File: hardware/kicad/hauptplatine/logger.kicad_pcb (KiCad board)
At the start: 4 copper layers, 121 x 121 mm, 4 parts

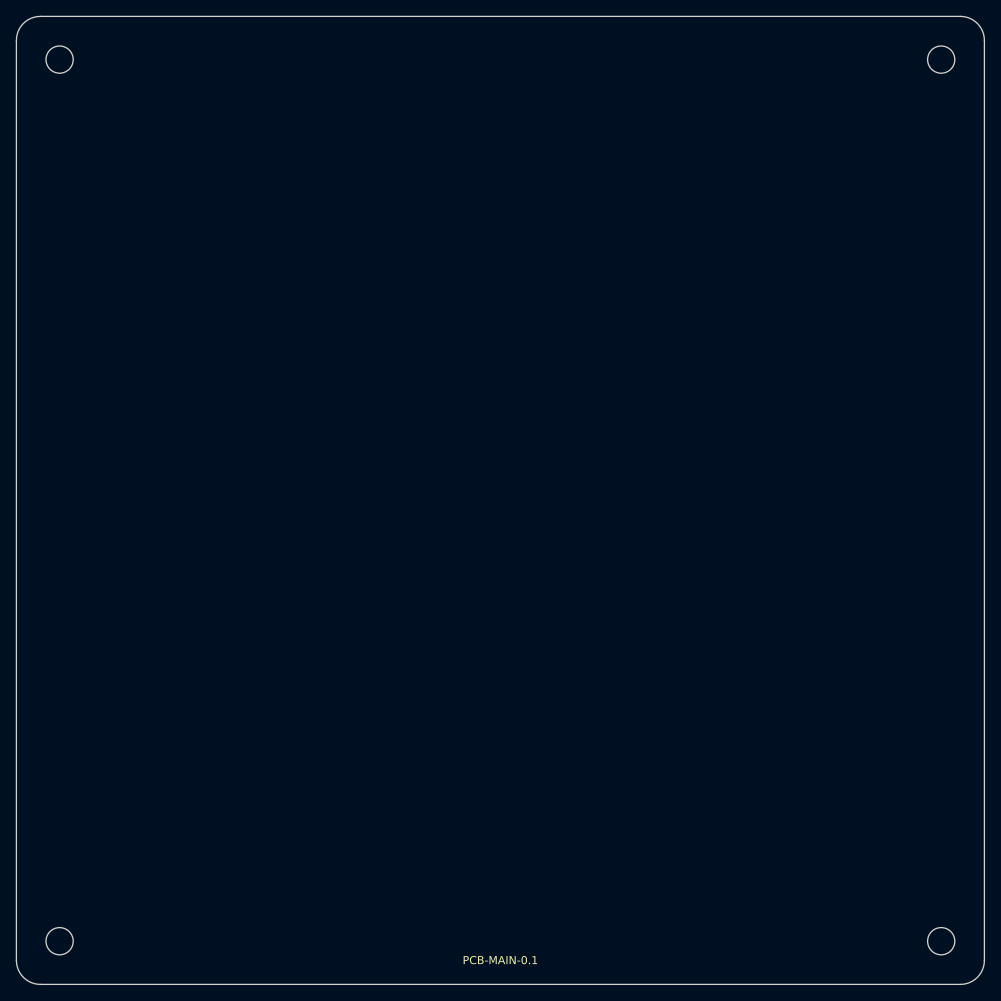
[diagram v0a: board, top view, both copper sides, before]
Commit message: update
"Hauptplatine grob platziert (platine_bestuecken.py, 139 Bauteile, Schaltplanabgleich 0); Gehäuse mit STEP geprüft: Lochbild bestätigt, Freiraum über Platine >= 44,3 mm (HW-03 erfüllt), Dombohrung Ø 2,4 mm korrigiert, Lichtleiter ca. 19,4 mm. Tests: ERC 0, Netzprüfung 178/178, alle_tests_linux.sh rc=0"
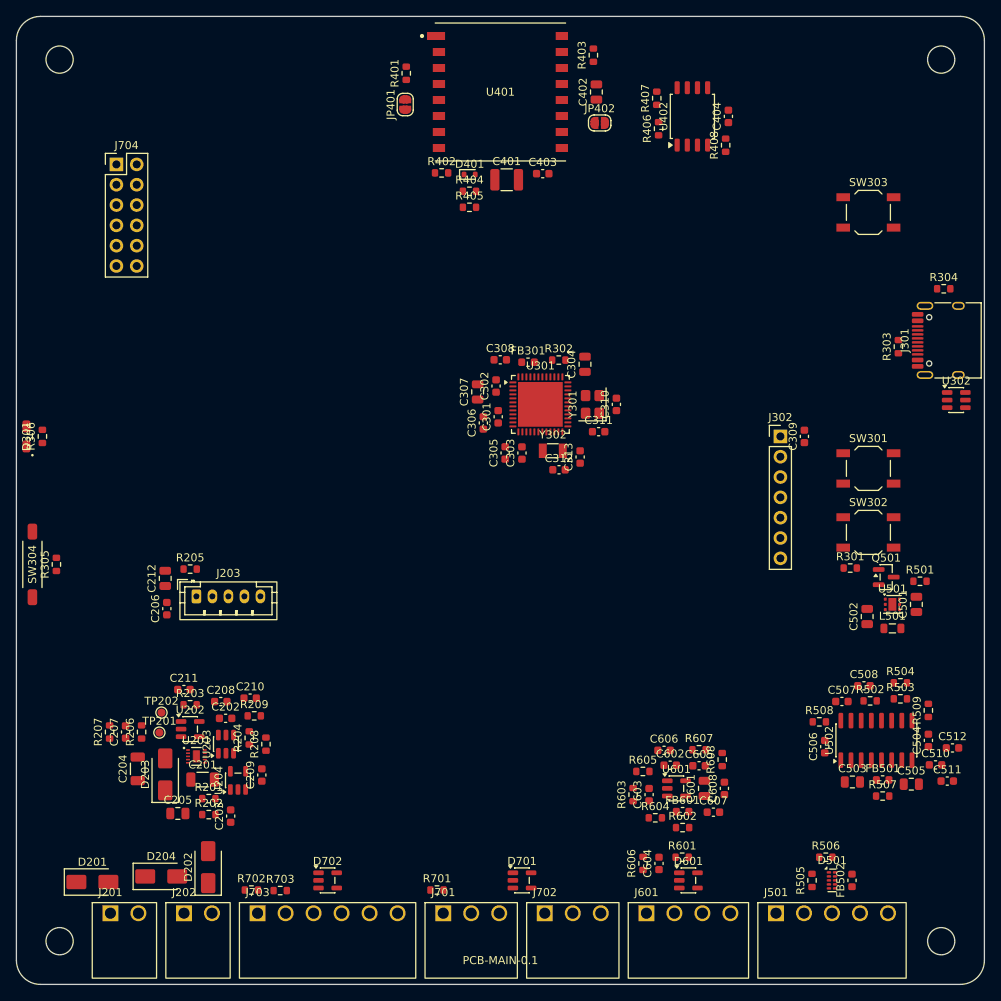
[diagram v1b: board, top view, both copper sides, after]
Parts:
- added C201: 4,7µ 50V X7R, Capacitor_SMD:C_1206_3216Metric, F.Cu at (62.8, 134.9)
- added C202: 100n 50V, Capacitor_SMD:C_0603_1608Metric, F.Cu at (65.7, 127.2)
- added C203: 100n, Capacitor_SMD:C_0603_1608Metric, F.Cu at (66.3, 139.5)
- added C204: 22µ 25V X5R, Capacitor_SMD:C_1206_3216Metric, F.Cu at (54.7, 133.6)
- added C205: 4,7µ, Capacitor_SMD:C_0805_2012Metric, F.Cu at (59.7, 139.1)
- added C206: 10n, Capacitor_SMD:C_0603_1608Metric, F.Cu at (58.3, 113.5)
- added C207: 100n, Capacitor_SMD:C_0603_1608Metric, F.Cu at (53.1, 128.9)
- added C208: 2,2µ 16V X7R, Capacitor_SMD:C_0603_1608Metric, F.Cu at (65.1, 125.1)
- added C209: 2,2µ 16V X7R, Capacitor_SMD:C_0603_1608Metric, F.Cu at (70.2, 134.3)
- added C210: 1n, Capacitor_SMD:C_0603_1608Metric, F.Cu at (68.7, 124.7)
- added C211: 1µ, Capacitor_SMD:C_0603_1608Metric, F.Cu at (60.4, 123.6)
- added C212: 4,7µ 16V X7R, Capacitor_SMD:C_0805_2012Metric, F.Cu at (58.1, 109.8)
- added C301: 100n, Capacitor_SMD:C_0603_1608Metric, F.Cu at (99.7, 89.5)
- added C302: 100n, Capacitor_SMD:C_0603_1608Metric, F.Cu at (99.5, 85.7)
- added C303: 100n, Capacitor_SMD:C_0603_1608Metric, F.Cu at (102.7, 94.1)
- added C304: 10µ 10V X5R, Capacitor_SMD:C_0805_2012Metric, F.Cu at (110.6, 83.0)
- added C305: 100n, Capacitor_SMD:C_0603_1608Metric, F.Cu at (100.6, 94.1)
- added C306: 1µ, Capacitor_SMD:C_0603_1608Metric, F.Cu at (97.9, 90.3)
- added C307: 4,7µ X7R, Capacitor_SMD:C_0805_2012Metric, F.Cu at (97.2, 86.4)
- added C308: 100n, Capacitor_SMD:C_0603_1608Metric, F.Cu at (100.0, 82.4)
- added C309: 100n, Capacitor_SMD:C_0603_1608Metric, F.Cu at (138.0, 92.0)
- added C310: 18p C0G, Capacitor_SMD:C_0603_1608Metric, F.Cu at (114.5, 88.0)
- added C311: 18p C0G, Capacitor_SMD:C_0603_1608Metric, F.Cu at (112.3, 91.4)
- added C312: 8,2p C0G, Capacitor_SMD:C_0603_1608Metric, F.Cu at (107.3, 96.2)
- added C313: 8,2p C0G, Capacitor_SMD:C_0603_1608Metric, F.Cu at (110.0, 94.6)
- added C401: 100µ 6,3V X5R, Capacitor_SMD:C_1210_3225Metric, F.Cu at (100.8, 59.9)
- added C402: 10µ 10V X5R, Capacitor_SMD:C_0805_2012Metric, F.Cu at (112.0, 49.0)
- added C403: 100n, Capacitor_SMD:C_0603_1608Metric, F.Cu at (105.3, 59.2)
- added C404: 100n, Capacitor_SMD:C_0603_1608Metric, F.Cu at (128.5, 52.0)
- added C501: 4,7µ 16V X5R, Capacitor_SMD:C_0805_2012Metric, F.Cu at (152.0, 113.0)
- added C502: 10µ 10V X5R, Capacitor_SMD:C_0805_2012Metric, F.Cu at (145.8, 114.5)
- added C503: 10µ 10V X5R, Capacitor_SMD:C_0805_2012Metric, F.Cu at (144.0, 135.2)
- added C504: 100n, Capacitor_SMD:C_0603_1608Metric, F.Cu at (153.5, 130.0)
- added C505: 10µ 10V X5R, Capacitor_SMD:C_0805_2012Metric, F.Cu at (151.4, 135.5)
- added C506: 100n, Capacitor_SMD:C_0603_1608Metric, F.Cu at (140.5, 130.8)
- added C507: 100n, Capacitor_SMD:C_0603_1608Metric, F.Cu at (142.7, 125.1)
- added C508: 100n, Capacitor_SMD:C_0603_1608Metric, F.Cu at (145.4, 123.2)
- added C510: 100n, Capacitor_SMD:C_0603_1608Metric, F.Cu at (154.4, 133.1)
- added C511: 10n C0G, Capacitor_SMD:C_0603_1608Metric, F.Cu at (155.9, 135.1)
- added C512: 10n C0G, Capacitor_SMD:C_0603_1608Metric, F.Cu at (156.5, 130.9)
- added C601: 22µ 10V X5R, Capacitor_SMD:C_0805_2012Metric, F.Cu at (125.5, 136.0)
- added C602: 100n, Capacitor_SMD:C_0603_1608Metric, F.Cu at (121.2, 133.1)
- added C603: 1µ, Capacitor_SMD:C_0603_1608Metric, F.Cu at (118.6, 136.8)
- added C604: 220n X7R, Capacitor_SMD:C_0603_1608Metric, F.Cu at (119.8, 145.4)
- added C605: 22n C0G, Capacitor_SMD:C_0603_1608Metric, F.Cu at (124.8, 133.2)
- added C606: 10n C0G, Capacitor_SMD:C_0603_1608Metric, F.Cu at (120.5, 131.2)
- added C607: 100n, Capacitor_SMD:C_0603_1608Metric, F.Cu at (126.6, 139.0)
- added C608: 10n C0G, Capacitor_SMD:C_0603_1608Metric, F.Cu at (128.0, 136.0)
- added D201: SS34, Diode_SMD:D_SMA, F.Cu at (49.0, 147.7)
- added D202: SS34, Diode_SMD:D_SMA, F.Cu at (63.5, 145.8)
- added D203: SS34, Diode_SMD:D_SMA, F.Cu at (58.1, 134.2)
- added D204: SMAJ12A, Diode_SMD:D_SMA, F.Cu at (57.6, 147.0)
- added D301: LTST-S220KGKT, Bienen:LED_Lite-On_LTST-S220_SideView, F.Cu at (40.8, 92.0)
- added D401: TVS 3,3V, Diode_SMD:D_SOD-523, F.Cu at (96.2, 59.3)
- added D501: TPD4E05U06DQAR, Package_SON:USON-10_2.5x1.0mm_P0.5mm, F.Cu at (141.4, 147.5)
- added D601: ESDS304DBVR, Package_TO_SOT_SMD:SOT-23-5, F.Cu at (123.5, 147.5)
- added D701: ESDS304DBVR, Package_TO_SOT_SMD:SOT-23-5, F.Cu at (102.7, 147.5)
- added D702: ESDS304DBVR, Package_TO_SOT_SMD:SOT-23-5, F.Cu at (78.4, 147.5)
- added FB301: 600R@100MHz, Inductor_SMD:L_0603_1608Metric, F.Cu at (103.5, 82.7)
- added FB501: 600R@100MHz, Inductor_SMD:L_0603_1608Metric, F.Cu at (147.8, 134.9)
- added FB502: Ferrit ≤ 0,1 Ω, Inductor_SMD:L_0603_1608Metric, F.Cu at (143.9, 147.5)
- added FB601: 600R@100MHz, Inductor_SMD:L_0603_1608Metric, F.Cu at (122.8, 138.9)
- added J201: Solar 1, Bienen:DEGSON_15EDGRC-3.5-02P, F.Cu at (51.2, 151.6)
- added J202: Solar 2, Bienen:DEGSON_15EDGRC-3.5-02P, F.Cu at (60.4, 151.6)
- added J203: Akku (JST PH 5), Connector_JST:JST_PH_B5B-PH-K_1x05_P2.00mm_Vertical, F.Cu at (62.0, 112.0)
- added J301: USB-C, Connector_USB:USB_C_Receptacle_HRO_TYPE-C-31-M-12, F.Cu at (156.2, 80.0)
- added J302: Debug (SWD + Serial1), Connector_PinHeader_2.54mm:PinHeader_1x07_P2.54mm_Vertical, F.Cu at (135.0, 92.0)
- added J501: Wägezelle, Bienen:DEGSON_15EDGRC-3.5-05P, F.Cu at (134.4, 151.6)
- added J601: Mikrofon, Bienen:DEGSON_15EDGRC-3.5-04P, F.Cu at (118.2, 151.6)
- added J701: DS18B20 Nr. 1, Bienen:DEGSON_15EDGRC-3.5-03P, F.Cu at (92.8, 151.6)
- added J702: DS18B20 Nr. 2, Bienen:DEGSON_15EDGRC-3.5-03P, F.Cu at (105.5, 151.6)
- added J703: BME280, Bienen:DEGSON_15EDGRC-3.5-06P, F.Cu at (69.6, 151.6)
- added J704: Erweiterung, Connector_PinHeader_2.54mm:PinHeader_2x06_P2.54mm_Vertical, F.Cu at (52.0, 58.0)
- added JP401: TXEN, Jumper:SolderJumper-2_P1.3mm_Open_RoundedPad1.0x1.5mm, F.Cu at (88.1, 50.5)
- added JP402: RXEN, Jumper:SolderJumper-2_P1.3mm_Open_RoundedPad1.0x1.5mm, F.Cu at (112.4, 52.8)
- added L501: 1µ, Inductor_SMD:L_0805_2012Metric, F.Cu at (149.0, 116.0)
- added Q501: S8550, Package_TO_SOT_SMD:SOT-23, F.Cu at (148.2, 109.6)
- added R201: 3,3M, Resistor_SMD:R_0603_1608Metric, F.Cu at (63.5, 137.3)
- added R202: 470k, Resistor_SMD:R_0603_1608Metric, F.Cu at (63.5, 139.3)
- added R203: 2,0k 1%, Resistor_SMD:R_0603_1608Metric, F.Cu at (61.2, 125.5)
- added R204: 130k 1%, Resistor_SMD:R_0603_1608Metric, F.Cu at (68.6, 129.7)
- added R205: 100k, Resistor_SMD:R_0603_1608Metric, F.Cu at (61.2, 108.6)
- added R206: 2,2M, Resistor_SMD:R_0603_1608Metric, F.Cu at (55.1, 128.9)
- added R207: 2,2M, Resistor_SMD:R_0603_1608Metric, F.Cu at (51.1, 128.9)
- added R208: 100k, Resistor_SMD:R_0603_1608Metric, F.Cu at (70.7, 130.5)
- added R209: 0, Resistor_SMD:R_0603_1608Metric, F.Cu at (69.2, 126.9)
- added R301: 10k, Resistor_SMD:R_0603_1608Metric, F.Cu at (143.7, 108.5)
- added R302: 10k, Resistor_SMD:R_0603_1608Metric, F.Cu at (107.3, 82.5)
- added R303: 5,1k, Resistor_SMD:R_0603_1608Metric, F.Cu at (149.7, 80.8)
- added R304: 5,1k, Resistor_SMD:R_0603_1608Metric, F.Cu at (155.4, 73.5)
- added R305: 100k, Resistor_SMD:R_0603_1608Metric, F.Cu at (44.5, 108.0)
- added R306: 1k, Resistor_SMD:R_0603_1608Metric, F.Cu at (42.8, 92.0)
- added R401: 33, Resistor_SMD:R_0603_1608Metric, F.Cu at (88.2, 46.6)
- added R402: 33, Resistor_SMD:R_0603_1608Metric, F.Cu at (92.7, 59.1)
- added R403: 33, Resistor_SMD:R_0603_1608Metric, F.Cu at (111.6, 44.3)
- added R404: 33, Resistor_SMD:R_0603_1608Metric, F.Cu at (96.1, 61.4)
- added R405: 100k, Resistor_SMD:R_0603_1608Metric, F.Cu at (96.1, 63.4)
- added R406: 100k, Resistor_SMD:R_0603_1608Metric, F.Cu at (119.8, 53.5)
- added R407: 10k, Resistor_SMD:R_0603_1608Metric, F.Cu at (119.5, 49.7)
- added R408: 10k, Resistor_SMD:R_0603_1608Metric, F.Cu at (128.2, 55.6)
- added R501: 100k, Resistor_SMD:R_0603_1608Metric, F.Cu at (152.4, 110.1)
- added R502: 100k, Resistor_SMD:R_0603_1608Metric, F.Cu at (146.2, 125.1)
- added R503: 20k 1%, Resistor_SMD:R_0603_1608Metric, F.Cu at (150.0, 124.8)
- added R504: 8,2k 1%, Resistor_SMD:R_0603_1608Metric, F.Cu at (150.0, 122.8)
- added R505: 100, Resistor_SMD:R_0603_1608Metric, F.Cu at (138.9, 147.5)
- added R506: 100, Resistor_SMD:R_0603_1608Metric, F.Cu at (140.7, 144.6)
- added R507: 0, Resistor_SMD:R_0603_1608Metric, F.Cu at (147.8, 137.0)
- added R508: 1k, Resistor_SMD:R_0603_1608Metric, F.Cu at (139.9, 127.7)
- added R509: 1k, Resistor_SMD:R_0603_1608Metric, F.Cu at (153.5, 126.2)
- added R601: 100, Resistor_SMD:R_0603_1608Metric, F.Cu at (122.7, 144.6)
- added R602: 47, Resistor_SMD:R_0603_1608Metric, F.Cu at (122.8, 140.9)
- added R603: 47k, Resistor_SMD:R_0603_1608Metric, F.Cu at (116.6, 136.8)
- added R604: 47k, Resistor_SMD:R_0603_1608Metric, F.Cu at (119.4, 139.7)
- added R605: 33k, Resistor_SMD:R_0603_1608Metric, F.Cu at (117.8, 133.9)
- added R606: 9,1k 1%, Resistor_SMD:R_0603_1608Metric, F.Cu at (117.8, 145.4)
- added R607: 9,1k 1%, Resistor_SMD:R_0603_1608Metric, F.Cu at (124.8, 131.2)
- added R608: 3,3k, Resistor_SMD:R_0603_1608Metric, F.Cu at (127.7, 132.4)
- added R701: 4,7k, Resistor_SMD:R_0603_1608Metric, F.Cu at (92.1, 148.7)
- added R702: 1,8k, Resistor_SMD:R_0603_1608Metric, F.Cu at (68.9, 148.7)
- added R703: 1,8k, Resistor_SMD:R_0603_1608Metric, F.Cu at (72.5, 148.8)
- added SW301: Reset, Button_Switch_SMD:SW_SPST_TL3342, F.Cu at (146.0, 96.0)
- added SW302: BOOT, Button_Switch_SMD:SW_SPST_TL3342, F.Cu at (146.0, 104.0)
- added SW303: Service, Button_Switch_SMD:SW_SPST_TL3342, F.Cu at (146.0, 64.0)
- added SW304: MRS03-B-3, Bienen:MiRelay_MRS03_J-Lead_8.5x2.1mm, F.Cu at (41.5, 108.0)
- added TP201: STAT1, TestPoint:TestPoint_Pad_D1.0mm, F.Cu at (57.4, 129.0)
- added TP202: STAT2, TestPoint:TestPoint_Pad_D1.0mm, F.Cu at (57.6, 126.5)
- added U201: BQ25185DLHR, Bienen:WSON-10-1EP_2.2x2mm_DLH0010A, F.Cu at (62.0, 132.0)
- added U202: RT9080-33GJ5, Package_TO_SOT_SMD:TSOT-23-5, F.Cu at (61.2, 128.6)
- added U203: TPS22917DBV, Package_TO_SOT_SMD:SOT-23-6, F.Cu at (65.7, 130.5)
- added U204: TPS70933DBV, Package_TO_SOT_SMD:SOT-23-5, F.Cu at (67.2, 135.0)
- added U301: STM32F411CEU6, Package_DFN_QFN:QFN-48-1EP_7x7mm_P0.5mm_EP5.6x5.6mm, F.Cu at (105.0, 88.0)
- added U302: USBLC6-2SC6, Package_TO_SOT_SMD:SOT-23-6, F.Cu at (157.0, 87.5)
- added U401: Ra-01SH, Bienen:Ai-Thinker_Ra-01SH, F.Cu at (100.0, 49.0)
- added U402: 64 Mbit SOIC-8 208 mil, Package_SO:SOIC-8_5.3x5.3mm_P1.27mm, F.Cu at (124.0, 52.0)
- added U501: TPS61240DRVR, Package_SON:WSON-6-1EP_2x2mm_P0.65mm_EP1x1.6mm, F.Cu at (149.0, 113.0)
- added U502: HX711, Package_SO:SOIC-16_3.9x9.9mm_P1.27mm, F.Cu at (147.0, 130.0)
- added U601: TLV9001IDBVR, Package_TO_SOT_SMD:SOT-23-5, F.Cu at (122.0, 136.0)
- added Y301: 25MHz 12pF, Crystal:Crystal_SMD_3225-4Pin_3.2x2.5mm, F.Cu at (111.5, 88.0)
- added Y302: 32,768k 7pF, Crystal:Crystal_SMD_3215-2Pin_3.2x1.5mm, F.Cu at (106.6, 93.8)

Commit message: Update
git commit -m "Feinplatzierung STM32/Ra-01SH/TPS61240, 13 Thermal-Vias, GND-Fläche L2 (platine_fein.py); DRC 0 Verstöße, Schaltplanabgleich 0"
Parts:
- moved R301 45.8 mm to (105.7, 82.9)
- moved C309 41.9 mm to (96.1, 93.2)
- moved R405 27.3 mm to (115.3, 44.0)
- moved C402 25.6 mm to (86.6, 46.0)
- moved R401 24.2 mm to (112.2, 50.0), turned to 0 degrees
- moved R404 23.7 mm to (112.2, 44.0)
- moved R402 22.5 mm to (112.2, 48.0)
- moved C401 22.1 mm to (83.6, 46.0), turned to 90 degrees
- moved C310 21.6 mm to (93.0, 90.0)
- moved C403 21.1 mm to (88.8, 46.0), turned to 90 degrees
- moved C311 19.9 mm to (93.0, 86.4), turned to 90 degrees
- moved C312 19.3 mm to (97.3, 79.7), turned to 90 degrees
- moved C313 18.0 mm to (99.8, 79.7)
- moved Y301 14.9 mm to (96.6, 88.2)
- moved Y302 13.8 mm to (98.6, 82.5)
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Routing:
- net GND: vias 0 -> 13
- added copper zone on In1.Cu, net GND

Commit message: Update
Versorgungslage L3: +3V3-Fläche mit Arm zu den Reglern, GND-Füllung (platine_lagen.py); DRC 0, Schaltplanabgleich 0
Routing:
- added copper zone on In2.Cu, net +3V3
- added copper zone on In2.Cu, net GND
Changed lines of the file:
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@@
+		)
+	)
+	(zone
+		(net "+3V3")
+		(layer "In2.Cu")
+		(name "P3V3_L3")
+		(hatch edge 0.5)
+		(priority 1)
+		(connect_pads
+			(clearance 0.2)
+		)
+		(min_thickness 0.2)
+		(fill yes
+			(thermal_gap 0.25)
+			(thermal_bridge_width 0.3)
+			(island_removal_mode 0)
+		)
+		(polygon
+			(pts
+				(xy 40 40) (xy 160 40) (xy 160 108) (xy 76 108) (xy 76 138) (xy 52 138) (xy 52 118) (xy 40 118)
+			)
+		)
+	)
+	(zone
+		(net "GND")
+		(layer "In2.Cu")
+		(name "GND_L3")
+		(hatch edge 0.5)
+		(connect_pads
+			(clearance 0.2)
+		)
+		(min_thickness 0.2)
+		(fill yes
+			(thermal_gap 0.25)
+			(thermal_bridge_width 0.3)
+			(island_removal_mode 0)
+		)
+		(polygon
+			(pts
+				(xy 40 40) (xy 160 40) (xy 160 160) (xy 40 160)
+			)
 		)
 	)

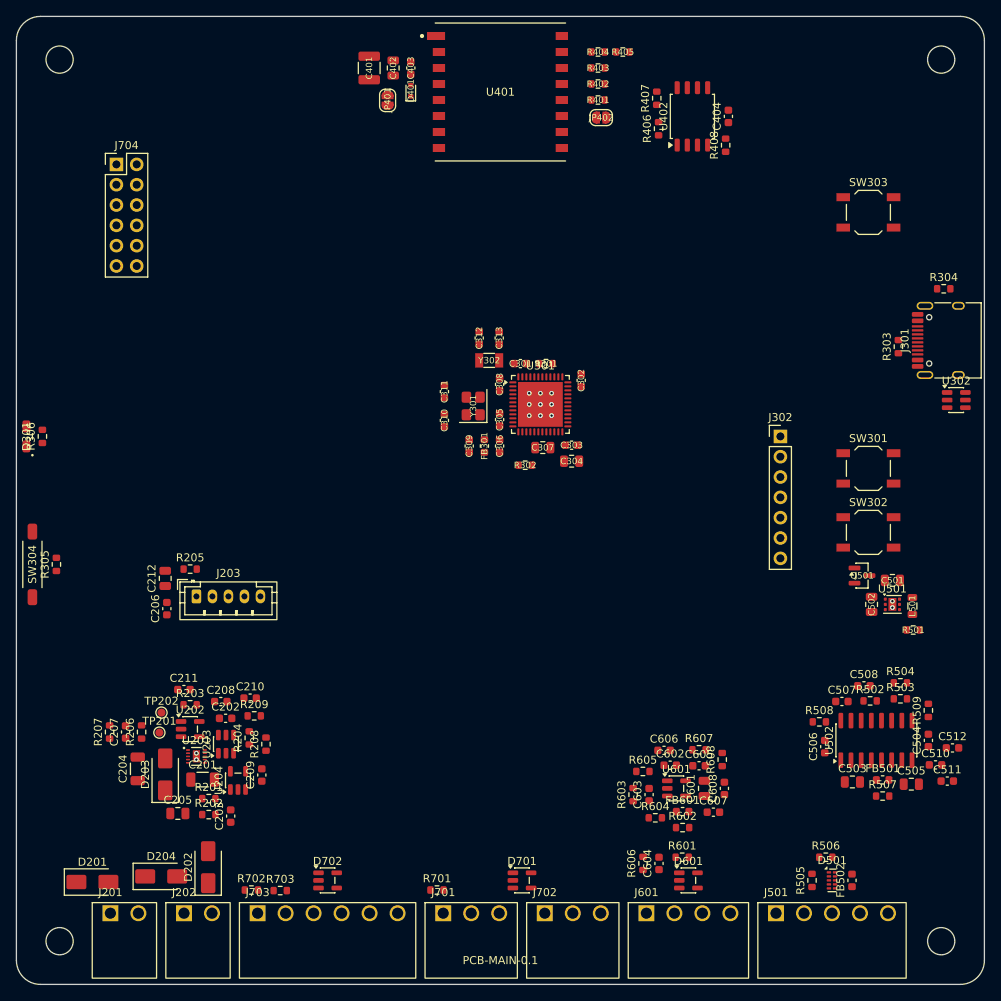
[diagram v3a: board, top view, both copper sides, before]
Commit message: Update
Lage L3 (+3V3/GND) und Fanout aller GND-/+3V3-Pads zu den Innenlagen (platine_lagen.py, platine_fanout.py); DRC 0, Schaltplanabgleich 0, offene Verbindungen 202
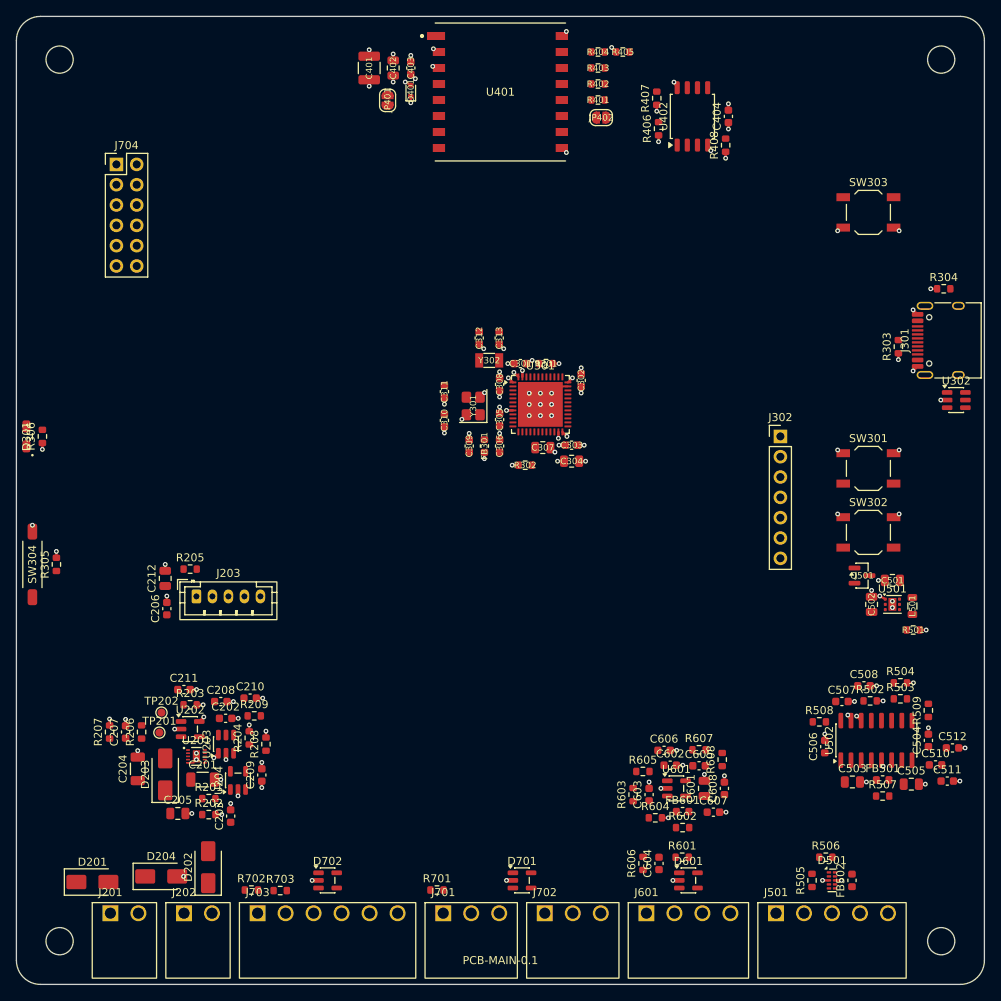
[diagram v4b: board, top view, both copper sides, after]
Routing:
- net GND: track 0.00 -> 71.2 mm, vias 13 -> 100
- net +3V3: track 0.00 -> 24.8 mm, vias 0 -> 31

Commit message: HW-06: Akku auf der Hauptplatine (Blatt Akku, Akku-Platine entfällt); HW-05: USB mit VBUS-Erkennung an PB13; Routing-Werkzeuge; Aufräumen: Restbezüge Akku-Platine, README-Stand; ERC 0, Netzprüfung 168/168, Pin/Footprint 0; Platine platziert, nicht geroutet
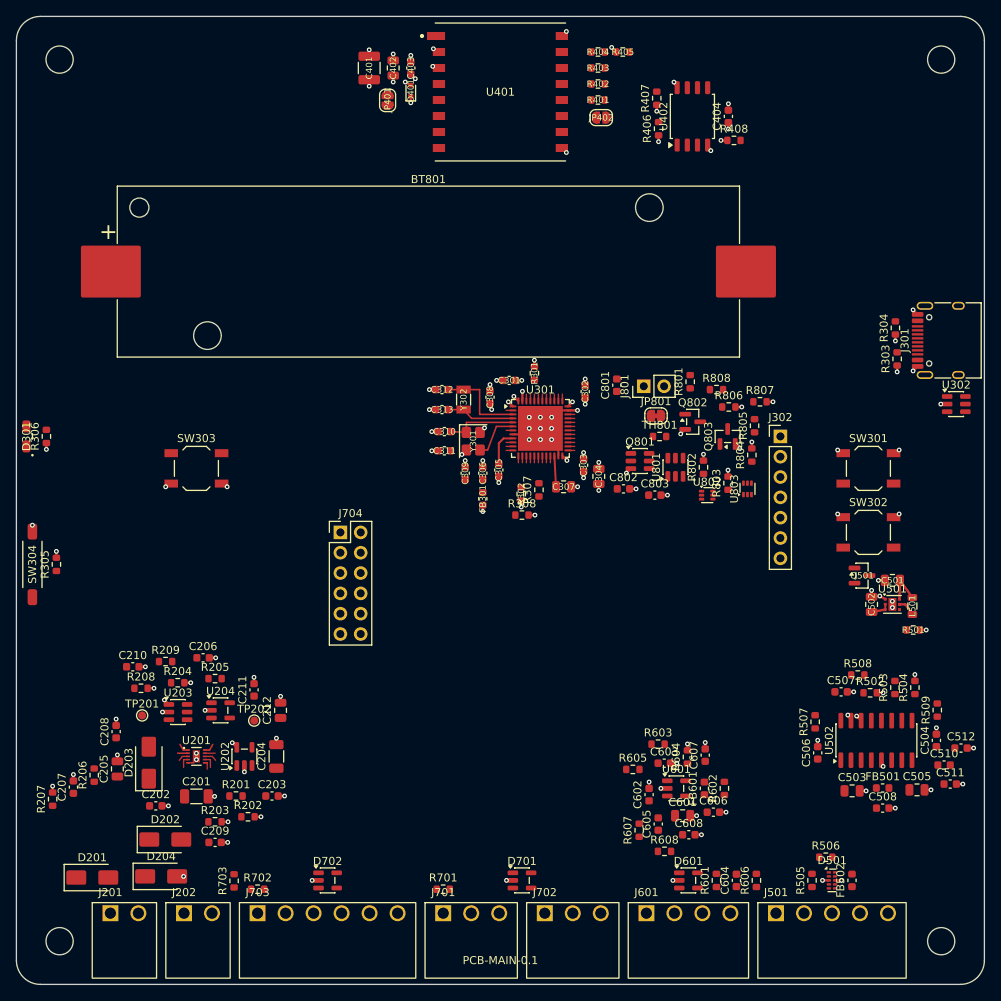
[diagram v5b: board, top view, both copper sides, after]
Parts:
- removed J203: Akku (JST PH 5), Connector_JST:JST_PH_B5B-PH-K_1x05_P2.00mm_Vertical
- added BT801: 18650 3,6 V, Battery:BatteryHolder_Keystone_1042_1x18650, F.Cu at (91.0, 71.4)
- added C801: 100n, Capacitor_SMD:C_0603_1608Metric, F.Cu at (114.5, 85.6)
- added C802: 100n, Capacitor_SMD:C_0603_1608Metric, F.Cu at (115.4, 98.6)
- added C803: 100n, Capacitor_SMD:C_0603_1608Metric, F.Cu at (119.3, 99.3)
- added J801: Strommessung, Connector_PinHeader_2.54mm:PinHeader_1x02_P2.54mm_Vertical, F.Cu at (117.9, 85.7)
- added JP801: Messbrücke B+, Jumper:SolderJumper-2_P1.3mm_Bridged_RoundedPad1.0x1.5mm, F.Cu at (119.5, 89.4)
- added Q801: FS8205, Package_TO_SOT_SMD:SOT-23-6, F.Cu at (117.5, 95.1)
- added Q802: AO3400A, Package_TO_SOT_SMD:SOT-23, F.Cu at (124.0, 90.2)
- added Q803: AO3400A, Package_TO_SOT_SMD:SOT-23, F.Cu at (128.4, 92.0)
- added R307: 33k, Resistor_SMD:R_0603_1608Metric, F.Cu at (104.8, 98.7)
- added R308: 82k, Resistor_SMD:R_0603_1608Metric, F.Cu at (102.7, 101.8)
- added R801: 100, Resistor_SMD:R_0603_1608Metric, F.Cu at (123.7, 85.2)
- added R802: 2k, Resistor_SMD:R_0603_1608Metric, F.Cu at (125.4, 95.9)
- added R803: 2,49k 1%, Resistor_SMD:R_0603_1608Metric, F.Cu at (128.5, 97.8)
- added R804: 18,7k 1%, Resistor_SMD:R_0603_1608Metric, F.Cu at (131.4, 94.3)
- added R805: 100k, Resistor_SMD:R_0603_1608Metric, F.Cu at (131.8, 90.7)
- added R806: 2,49k 1%, Resistor_SMD:R_0603_1608Metric, F.Cu at (128.5, 88.3)
- added R807: 18,7k 1%, Resistor_SMD:R_0603_1608Metric, F.Cu at (132.4, 87.7)
- added R808: 100k, Resistor_SMD:R_0603_1608Metric, F.Cu at (127.0, 86.1)
- added TH801: 10k B3435, Resistor_SMD:R_0603_1608Metric, F.Cu at (119.9, 92.0)
- added U801: HY2111-GB, Package_TO_SOT_SMD:SOT-23-6, F.Cu at (121.9, 95.9)
- added U802: TMP390A2DRL, Package_TO_SOT_SMD:SOT-563, F.Cu at (125.9, 99.3)
- added U803: TMP390A2DRL, Package_TO_SOT_SMD:SOT-563, F.Cu at (130.9, 98.6)
- moved SW303 89.9 mm to (62.0, 96.0)
- moved J704 53.9 mm to (80.0, 104.0)
- moved C212 21.9 mm to (72.5, 126.2)
- moved C204 17.4 mm to (72.0, 132.0)
- moved R208 17.1 mm to (55.1, 123.5), turned to 0 degrees
- moved C508 15.5 mm to (147.8, 138.5)
- moved C210 15.2 mm to (54.0, 120.8)
- moved R203 15.0 mm to (64.3, 140.2)
- moved R606 14.3 mm to (132.0, 147.5)
- moved R205 14.0 mm to (64.3, 122.3)
- moved C202 14.0 mm to (56.9, 138.2)
- moved C208 13.6 mm to (52.0, 128.9), turned to 90 degrees
- moved R608 13.6 mm to (120.5, 143.9), turned to 0 degrees
- moved R209 13.0 mm to (58.1, 120.1)
- moved R507 12.5 mm to (139.3, 127.7), turned to 90 degrees
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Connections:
- net /Versorgung/CE_LADEN renamed CE_LADEN
- net /Versorgung/TMP_VCC renamed TMP_VCC
- net /Versorgung/VBAT renamed VBAT
- J704 pad 11: EXT_PB13 -> unconnected-(J704-Pin_11-Pad11)
- U201 pad 6: /Versorgung/NTC -> NTC
- U301 pad 26: EXT_PB13 -> /MCU/VBUS_SENSE
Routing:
- net /MCU/LSE_IN: track 0.00 -> 11.2 mm
- net GND: track 71.2 -> 81.7 mm, vias 100 -> 110
- net /MCU/HSE_IN: track 0.00 -> 9.04 mm
- net /MCU/LSE_OUT: track 0.00 -> 8.57 mm
- net SYS: track 0.00 -> 6.40 mm
- net /MCU/HSE_OUT: track 0.00 -> 6.16 mm
- net /MCU/VDDA: track 0.00 -> 4.58 mm
- net /MCU/VCAP: track 0.00 -> 3.87 mm
- net /Waage/5V_WAAGE: track 0.00 -> 2.39 mm
- net /Waage/L_5V: track 0.00 -> 2.28 mm
- net /Versorgung/ILIM: track 0.00 -> 1.70 mm
- net /Versorgung/ISET: track 0.00 -> 1.59 mm
- net CE_LADEN: track 0.00 -> 1.55 mm
- net /Versorgung/VIN_LADER: track 0.00 -> 1.41 mm
- net /Versorgung/LADE_STAT2: track 0.00 -> 1.34 mm
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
